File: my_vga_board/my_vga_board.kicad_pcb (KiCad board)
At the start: 4 copper layers, 85 x 56 mm, 71 parts, among them J1 AudioJack3, J2 AudioJack3, J3 Micro_SD_Card, J4 L77HDE15SD1CH4F, J5 USB_B_Micro, J6 Conn_01x02, J7 Conn_02x03_Odd_Even, SW1 SW_Push, SW2 SW_Push, SW3 SW_Push, SW4 SW_Push, U1 TLV70033_SOT23-5, U2 Pico, U3 NC7WZ16P6X, U4 PCM5101A

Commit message: updated commit
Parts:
- removed C1, C2: 1u, Capacitor_SMD:C_0603_1608Metric
- removed C10, C16, C19, C3: 10u, Capacitor_SMD:C_0603_1608Metric
- removed C11, C9: 2.2u, Capacitor_SMD:C_0603_1608Metric
- removed C12, C13, C4, C5, C6, C7, C8: 100n, Capacitor_SMD:C_0402_1005Metric
- removed C14, C15, C21: 47u, Capacitor_SMD:C_0805_2012Metric
- removed C17, C18: 2.2n, Capacitor_SMD:C_0402_1005Metric
- removed D1: MBR120, RPi_Pico:MBR120_SOD-123
- removed H1, H2, H3, H4: MountingHole, MountingHole:MountingHole_2.7mm_M2.5
- removed J1, J2: AudioJack3, RPi_Pico:CUI_SJ-3523-audio-jack
- removed J3: Micro_SD_Card, Connector_Card:microSD_HC_Molex_104031-0811
- removed J5: USB_B_Micro, RPi_Pico:USB_Micro-B_Amphenol_10103594-0001LF_Horizontal_modified
- removed J6: Conn_01x02, Connector_PinHeader_2.54mm:PinHeader_1x02_P2.54mm_Vertical
- removed J7: Conn_02x03_Odd_Even, Connector_PinHeader_2.54mm:PinHeader_2x04_P2.54mm_Vertical
- removed R1, R2: 220, Resistor_SMD:R_0402_1005Metric
- removed R20, R21, R22: 1k, Resistor_SMD:R_0402_1005Metric
- removed R23, R24: 10k, Resistor_SMD:R_0402_1005Metric
- removed R3, R4: 100, Resistor_SMD:R_0402_1005Metric
- removed R5, R6: 470, Resistor_SMD:R_0402_1005Metric
- removed R7, R8: 1.8K, Resistor_SMD:R_0402_1005Metric
- removed R9: DNF, Resistor_SMD:R_0402_1005Metric
- removed SW1, SW2, SW3, SW4: SW_Push, Button_Switch_SMD:SW_Push_1P1T_NO_Vertical_Wuerth_434133025816
- removed U2: Pico, RPi_Pico:RPi_Pico_SMD_TH
- removed U3: NC7WZ16P6X, Package_TO_SOT_SMD:SOT-363_SC-70-6
- removed U4: PCM5101A, Package_SO:TSSOP-20_4.4x6.5mm_P0.65mm
- U1: value TLV70033_SOT23-5 -> Pico; footprint Package_TO_SOT_SMD:SOT-23-5 -> RPi_Pico:RPi_Pico_SMD_TH
- moved R10 63.8 mm to (87.8, 76.4), turned to 0 degrees
- moved R30 62.7 mm to (84.9, 108.0)
- moved R40 61.4 mm to (165.1, 52.4)
- moved R11 61.1 mm to (84.9, 106.0), turned to 0 degrees
- moved R28 40.3 mm to (84.9, 84.3)
- moved R29 38.5 mm to (87.8, 82.4)
- moved R26 38.4 mm to (84.9, 86.3)
- moved R38 33.7 mm to (84.9, 80.4)
- moved R36 33.6 mm to (87.8, 80.4)
- moved R37 32.1 mm to (90.7, 76.4)
- moved R35 31.3 mm to (84.9, 76.4)
- moved R34 31.2 mm to (84.9, 78.4)
- moved R31 30.9 mm to (84.9, 82.4)
- moved R39 30.9 mm to (87.8, 78.4)
- moved R27 28.2 mm to (93.6, 78.4)
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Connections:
- J4 pad 11: Net-(J4-Pad11) -> unconnected-(J4-Pad11)
- J4 pad 12: Net-(J4-Pad12) -> unconnected-(J4-Pad12)
- J4 pad 15: Net-(J4-Pad15) -> unconnected-(J4-Pad15)
- J4 pad 4: Net-(J4-Pad4) -> unconnected-(J4-Pad4)
- J4 pad 9: Net-(J4-Pad9) -> unconnected-(J4-Pad9)
- U1 pad 1: /VSYS -> /GPIO0
- U1 pad 2: GND -> /GPIO1
- U1 pad 3: /VSYS -> GND
- U1 pad 4: Net-(U1-Pad4) -> /GPIO2
- U1 pad 5: +3.3VA -> /GPIO3
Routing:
- net (no net): track 0.00 -> 89.5 mm
- net /GPIO5: track 81.2 -> 0.00 mm
- net /VSYNC: track 79.3 -> 0.00 mm
- net /HSYNC: track 74.2 -> 0.00 mm
- net Net-(R20-Pad2): track 59.0 -> 0.00 mm
- net GND: track 53.9 -> 0.00 mm, vias 66 -> 0
- net /GPIO18: track 46.9 -> 0.00 mm
- net /GPIO22: track 43.8 -> 0.00 mm
- net /GPIO19: track 40.1 -> 0.00 mm, vias 1 -> 0
- net Net-(R21-Pad2): track 37.5 -> 0.00 mm, vias 2 -> 0
- net /SWCLK: track 35.6 -> 0.00 mm
- net /GPIO12: track 6.59 -> 38.5 mm
- net /VGA_B: track 31.5 -> 0.00 mm, vias 1 -> 0
- net /RUN: track 31.5 -> 0.00 mm
- net /VGA_G: track 28.8 -> 0.00 mm
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- added copper zone on B.Cu, net (none)
- removed copper zone on B.Cu, net +3.3VA
- removed copper zone on B.Cu, net +3V3
- removed copper zone on F.Cu, net +5V
- removed copper zone on F.Cu, net /VSYS
- removed copper zone on F.Cu, net GND
- removed copper zone on F.Cu, net VBUS
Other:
- board outline removed
- net class Default removed
- board text removed: "A"
- board text removed: "B"
- board text removed: "C"
- board text removed: "DEBUG"
- board text removed: "GND"
- board text removed: "PCM"
- board text removed: "PWM"
- board text removed: "Pico"
- board text removed: "Power In"
- board text removed: "RPI-PVSA REV2"
- board text removed: "RUN"
- board text removed: "RX"
- board text removed: "SWCLK"
- board text removed: "SWDIO"
- board text removed: "TX"
- board text removed: "UART"
- board text removed: "USB"
- board text removed: "User Buttons"
- board text removed: "VGA"
- board text removed: "VGA, SD Card & Audio Demo Board for Pico (c) Raspberry Pi 2020"
- board text removed: "uSD Card"

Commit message: adding power circuit, some layout schtuff
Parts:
- added C1: 0.33uF, Capacitor_THT:CP_Radial_D5.0mm_P2.00mm, F.Cu at (170.5, 83.3)
- added C2: 0.1uF, Capacitor_THT:CP_Radial_D5.0mm_P2.00mm, F.Cu at (170.5, 90.9)
- added J1: Barrel_Jack, Connector_BarrelJack:BarrelJack_Horizontal, F.Cu at (169.0, 102.0)
- added U2: LM7805_TO220, Package_TO_SOT_THT:TO-220-3_Vertical, F.Cu at (172.5, 73.1)
- moved R10 86.8 mm to (167.4, 111.2)
- moved R11 82.8 mm to (167.4, 113.7)
- moved R30 63.6 mm to (134.4, 68.0)
- moved R40 59.7 mm to (134.4, 103.6)
- moved R36 57.3 mm to (134.4, 113.7)
- moved R38 57.0 mm to (134.4, 108.7)
- moved R37 55.8 mm to (134.4, 111.2)
- moved R39 54.2 mm to (134.4, 106.1)
- moved R31 52.0 mm to (134.4, 98.5)
- moved R34 51.0 mm to (134.4, 90.9)
- moved R35 50.9 mm to (134.4, 88.3)
- moved R28 50.7 mm to (134.4, 73.1)
- moved R26 50.1 mm to (134.4, 78.2)
- moved R29 48.0 mm to (134.4, 70.6)
- moved R32 47.0 mm to (134.4, 96.0)
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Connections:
- U1 pad 39: unconnected-(U1-Pad39) -> +5V
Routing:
- net (no net): track 89.5 -> 28.3 mm
- net GND: track 0.00 -> 57.6 mm
- net /GPIO7: track 0.00 -> 38.5 mm
- net /GPIO12: track 38.5 -> 0.00 mm
- net /GPIO9: track 0.00 -> 35.6 mm
- net unconnected-(U1-Pad25): track 17.1 -> 0.00 mm
- net unconnected-(U1-Pad24): track 15.0 -> 0.00 mm

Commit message: I don't know, some changes?
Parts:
- moved J4 2.10 mm to (109.0, 88.3)
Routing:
- net unconnected-(J4-Pad15): track 0.00 -> 20.2 mm
- net /VGA_R: track 20.2 -> 0.00 mm
- net (no net): track 28.3 -> 8.83 mm
- net GND: track 57.6 -> 77.1 mm
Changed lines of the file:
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@@
   )
   (footprint "RPi_Pico:DSUB-15-L77HDE15SD1CH4F" (layer "F.Cu")
-    (at 111.062831 88.34 90)
+    (at 108.96 88.34 90)
     (descr "15-pin D-Sub connector, horizontal/angled (90 deg), THT-mount, female, pitch 2.29x1.98mm, pin-PCB-offset 3.0300000000000002mm, distance of mounting holes 25mm, distance of mounting holes to PCB edge 4.9399999999999995mm, see https://disti-assets.s3.amazonaws.com/tonar/files/datasheets/16730.pdf")
     (tags "15-pin D-Sub connector horizontal angled 90deg THT female pitch 2.29x1.98mm pin-PCB-offset 3.0300000000000002mm mounting-holes-distance 25mm mounting-hole-offset 25mm")
@@
   (segment (start 110.7 86.4) (end 108.7 88.4) (width 0.15) (layer "B.Cu") (net 0))
   (segment (start 108.7 88.4) (end 108.7 94.4) (width 0.15) (layer "B.Cu") (net 0))
-  (segment (start 102.2 83.631998) (end 102.2 94.2) (width 0.15) (layer "B.Cu") (net 0))
-  (segment (start 108.8 78.1) (end 107.731998 78.1) (width 0.15) (layer "B.Cu") (net 0))
-  (segment (start 107.731998 78.1) (end 102.2 83.631998) (width 0.15) (layer "B.Cu") (net 0))
   (segment (start 174.489999 95.689999) (end 174.900001 96.100001) (width 0.15) (layer "B.Cu") (net 1))
   (segment (start 160.94 92.4) (end 160.84 92.3) (width 0.15) (layer "B.Cu") (net 1))
   (segment (start 156.577919 97.9) (end 157.097919 97.38) (width 0.15) (layer "B.Cu") (net 1))
   (segment (start 157.097919 97.38) (end 158.3 97.38) (width 0.15) (layer "B.Cu") (net 1))
+  (segment (start 102.2 83.631998) (end 102.2 94.2) (width 0.15) (layer "B.Cu") (net 1))
   (segment (start 161.689999 95.689999) (end 174.489999 95.689999) (width 0.15) (layer "B.Cu") (net 1))
   (segment (start 174.900001 96.100001) (end 175.2 96.4) (width 0.15) (layer "B.Cu") (net 1))
+  (segment (start 108.8 78.1) (end 107.731998 78.1) (width 0.15) (layer "B.Cu") (net 1))
   (segment (start 134.35 97.9) (end 156.577919 97.9) (width 0.15) (layer "B.Cu") (net 1))
   (segment (start 171.2 92.4) (end 160.94 92.4) (width 0.15) (layer "B.Cu") (net 1))
+  (segment (start 107.731998 78.1) (end 102.2 83.631998) (width 0.15) (layer "B.Cu") (net 1))
   (segment (start 160.84 94.84) (end 161.689999 95.689999) (width 0.15) (layer "B.Cu") (net 1))
   (segment (start 176.2 88.4) (end 175.2 88.4) (width 0.15) (layer "B.Cu") (net 1))
   (segment (start 175.2 88.4) (end 171.2 92.4) (width 0.15) (layer "B.Cu") (net 1))
   (segment (start 133.35 98.9) (end 134.35 97.9) (width 0.15) (layer "B.Cu") (net 1))
-  (segment (start 110.4 74.38) (end 107.47 71.45) (width 0.3) (layer "B.Cu") (net 11))
-  (segment (start 114.2 84.9) (end 110.4 81.1) (width 0.3) (layer "B.Cu") (net 11))
-  (segment (start 110.4 81.1) (end 110.4 74.38) (width 0.3) (layer "B.Cu") (net 11))
-  (segment (start 114.2 88.9) (end 114.2 84.9) (width 0.3) (layer "B.Cu") (net 11))
+  (segment (start 110.4 74.38) (end 107.47 71.45) (width 0.3) (layer "B.Cu") (net 4))
+  (segment (start 114.2 84.9) (end 110.4 81.1) (width 0.3) (layer "B.Cu") (net 4))
+  (segment (start 110.4 81.1) (end 110.4 74.38) (width 0.3) (layer "B.Cu") (net 4))
+  (segment (start 114.2 88.9) (end 114.2 84.9) (width 0.3) (layer "B.Cu") (net 4))
   (segment (start 128.27 97.697919) (end 130.667919 95.3) (width 0.15) (layer "B.Cu") (net 20))
   (segment (start 159.56 96.1) (end 160.84 97.38) (width 0.15) (layer "B.Cu") (net 20))

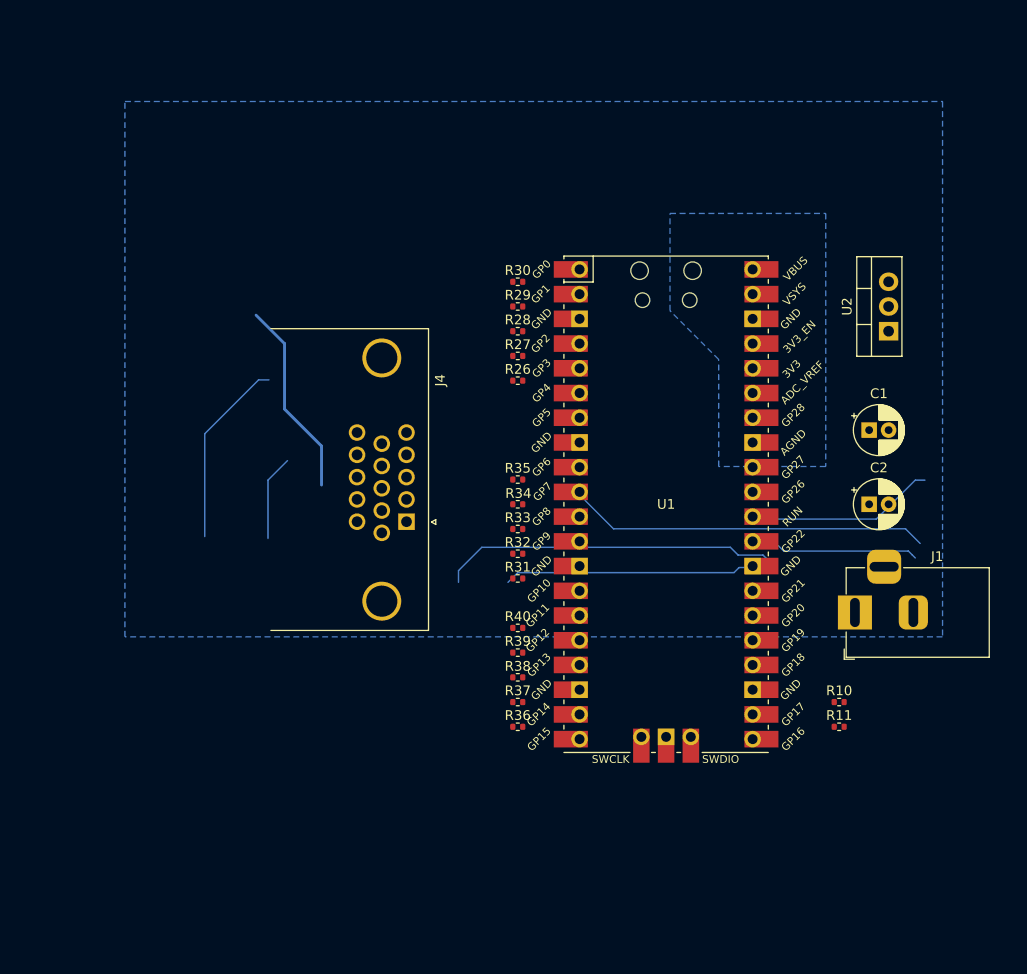
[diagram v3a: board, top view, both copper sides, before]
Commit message: better footprints for resistance
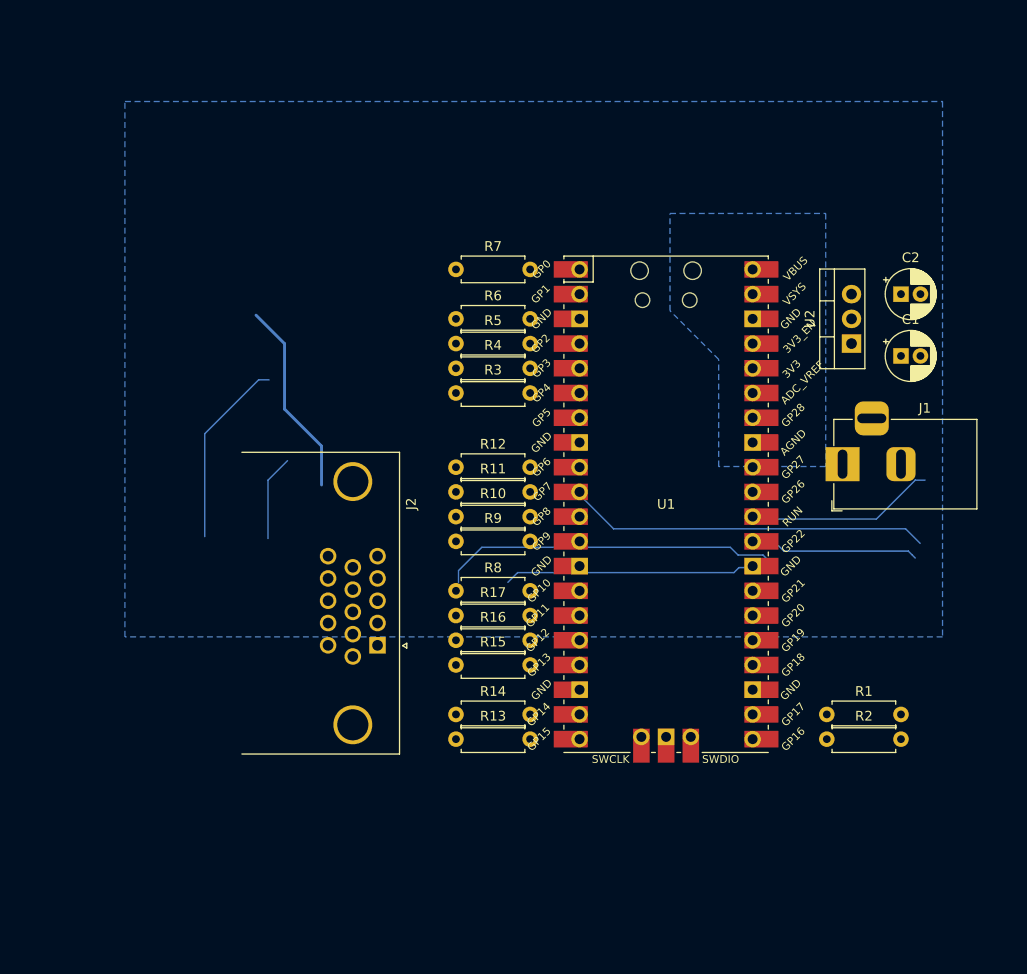
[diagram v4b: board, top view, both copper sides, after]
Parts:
- removed J4: L77HDE15SD1CH4F, RPi_Pico:DSUB-15-L77HDE15SD1CH4F
- removed R26, R31, R36: 499, Resistor_SMD:R_0402_1005Metric
- removed R27, R32, R37: 1k, Resistor_SMD:R_0402_1005Metric
- removed R28, R33, R38: 2k, Resistor_SMD:R_0402_1005Metric
- removed R29, R34, R39: 4.02k, Resistor_SMD:R_0402_1005Metric
- removed R30, R35, R40: 8.06k, Resistor_SMD:R_0402_1005Metric
- added J2: L77HDE15SD1CH4F, RPi_Pico:DSUB-15-L77HDE15SD1CH4F, F.Cu at (106.0, 101.0)
- added R1: 47, Resistor_THT:R_Axial_DIN0207_L6.3mm_D2.5mm_P7.62mm_Horizontal, F.Cu at (166.1, 112.5)
- added R12: 8.06k, Resistor_THT:R_Axial_DIN0207_L6.3mm_D2.5mm_P7.62mm_Horizontal, F.Cu at (128.0, 87.1)
- added R13: 499, Resistor_THT:R_Axial_DIN0207_L6.3mm_D2.5mm_P7.62mm_Horizontal, F.Cu at (128.0, 115.0)
- added R14: 1k, Resistor_THT:R_Axial_DIN0207_L6.3mm_D2.5mm_P7.62mm_Horizontal, F.Cu at (128.0, 112.5)
- added R15: 2k, Resistor_THT:R_Axial_DIN0207_L6.3mm_D2.5mm_P7.62mm_Horizontal, F.Cu at (128.0, 107.4)
- added R16: 4.02k, Resistor_THT:R_Axial_DIN0207_L6.3mm_D2.5mm_P7.62mm_Horizontal, F.Cu at (128.0, 104.8)
- added R17: 8.06k, Resistor_THT:R_Axial_DIN0207_L6.3mm_D2.5mm_P7.62mm_Horizontal, F.Cu at (128.0, 102.3)
- added R2: 47, Resistor_THT:R_Axial_DIN0207_L6.3mm_D2.5mm_P7.62mm_Horizontal, F.Cu at (166.1, 115.0)
- added R3: 499, Resistor_THT:R_Axial_DIN0207_L6.3mm_D2.5mm_P7.62mm_Horizontal, F.Cu at (128.0, 79.5)
- added R4: 1k, Resistor_THT:R_Axial_DIN0207_L6.3mm_D2.5mm_P7.62mm_Horizontal, F.Cu at (128.0, 76.9)
- added R5: 2k, Resistor_THT:R_Axial_DIN0207_L6.3mm_D2.5mm_P7.62mm_Horizontal, F.Cu at (128.0, 74.4)
- added R6: 4.02k, Resistor_THT:R_Axial_DIN0207_L6.3mm_D2.5mm_P7.62mm_Horizontal, F.Cu at (128.0, 71.8)
- added R7: 8.06k, Resistor_THT:R_Axial_DIN0207_L6.3mm_D2.5mm_P7.62mm_Horizontal, F.Cu at (128.0, 66.8)
- added R8: 499, Resistor_THT:R_Axial_DIN0207_L6.3mm_D2.5mm_P7.62mm_Horizontal, F.Cu at (128.0, 99.8)
- added R9: 1k, Resistor_THT:R_Axial_DIN0207_L6.3mm_D2.5mm_P7.62mm_Horizontal, F.Cu at (128.0, 94.7)
- R10: value 47 -> 2k; footprint Resistor_SMD:R_0402_1005Metric -> Resistor_THT:R_Axial_DIN0207_L6.3mm_D2.5mm_P7.62mm_Horizontal
- R11: value 47 -> 4.02k; footprint Resistor_SMD:R_0402_1005Metric -> Resistor_THT:R_Axial_DIN0207_L6.3mm_D2.5mm_P7.62mm_Horizontal
- moved R11 46.2 mm to (128.0, 89.6)
- moved R10 43.7 mm to (128.0, 92.2)
- moved C2 21.8 mm to (173.7, 69.3)
- moved J1 15.3 mm to (167.7, 86.8)
- moved C1 8.29 mm to (173.7, 75.6)
- moved U2 4.02 mm to (168.7, 74.4)
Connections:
- R10 pad 1: /VSYNC -> /VGA_G
- R10 pad 2: /GPIO17 -> /GPIO8
- R11 pad 1: /HSYNC -> /VGA_G
- R11 pad 2: /GPIO16 -> /GPIO7
- U1 pad 7: /GPIO5 -> unconnected-(U1-Pad7)
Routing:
- net unconnected-(J4-Pad15): track 20.2 -> 0.00 mm
- net (no net): track 8.83 -> 29.1 mm
- net /GPIO7: track 38.5 -> 55.5 mm
- net GND: track 77.1 -> 60.0 mm

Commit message: adding tracks!  Neat
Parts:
- moved J2 55.4 mm to (149.6, 135.3), turned to 180 degrees
- moved C1 12.0 mm to (165.5, 84.4), turned to -90 degrees
- moved J1 9.97 mm to (170.4, 77.2)
- moved C2 8.22 mm to (165.5, 69.3), turned to 90 degrees
- moved U2 6.06 mm to (165.4, 79.5)
- moved R1 5.59 mm to (171.7, 112.2), turned to 180 degrees
- moved R2 5.59 mm to (171.7, 115.3), turned to 180 degrees
- moved R6 2.29 mm to (128.0, 69.5)
- moved R15 0.76 mm to (128.0, 108.2)
- moved R8 0.76 mm to (128.0, 99.0)
- moved R9 0.76 mm to (128.0, 95.5)
- moved R12 0.76 mm to (128.0, 86.3)
- moved R5 0.51 mm to (128.0, 73.9)
- moved R3 0.51 mm to (128.0, 80.0)
- moved R11 0.25 mm to (128.0, 89.4)
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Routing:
- net /VGA_R: track 0.00 -> 76.5 mm
- net GND: track 60.0 -> 0.00 mm
- net /VGA_G: track 0.00 -> 54.6 mm
- net /GPIO7: track 55.5 -> 5.19 mm
- net /VSYNC: track 0.00 -> 44.5 mm
- net /VGA_B: track 0.00 -> 37.0 mm
- net /HSYNC: track 0.00 -> 32.1 mm
- net /GPIO9: track 35.6 -> 5.40 mm
- net (no net): track 29.1 -> 0.00 mm
- net +5V: track 0.00 -> 12.2 mm
- net Net-(C1-Pad1): track 0.00 -> 10.9 mm
- net /GPIO17: track 0.00 -> 5.69 mm
- net /GPIO16: track 0.00 -> 5.69 mm
- net /GPIO13: track 0.00 -> 5.40 mm
- net /GPIO10: track 0.00 -> 5.40 mm
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- removed copper zone on B.Cu, net (none)
- removed copper zone on In1.Cu, net GND
- removed copper zone on In2.Cu, net GND
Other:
- board outline added: 53.3 x 96 mm
- rule pad_to_mask_clearance: 0.051 -> 0.0508
